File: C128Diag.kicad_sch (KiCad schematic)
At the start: 29 parts, among them U1 4066, U10 74LS04, U11 74LS04, U12 74LS10, U13 27128, U14 C64-Exp-Port, U2 4066, U3 4066, U4 NE555P, U5 74LS245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

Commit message: Tracing traces and reconstructing schematics.
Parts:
- added J1: CP1, Connector_PinHeader_2.54mm:PinHeader_1x05_P2.54mm_Vertical, symbol Connector_Generic:Conn_01x05
- added J2: CP2, Connector_PinHeader_2.54mm:PinHeader_1x05_P2.54mm_Vertical, symbol Connector_Generic:Conn_01x05
- added J3: KB, Connector_PinHeader_2.54mm:PinHeader_1x13_P2.54mm_Vertical, symbol Connector_Generic:Conn_01x13
- added JU1, JU2, JU3, JU4, JU5: Jumper_2_Open, C128Diag:Jumper, symbol Jumper:Jumper_2_Open
- added P1: 1k, Potentiometer_THT:Potentiometer_Bourns_3339P_Vertical, symbol Device:R_Potentiometer
- added R1: 150, Resistor_THT:R_Axial_DIN0309_L9.0mm_D3.2mm_P12.70mm_Horizontal, symbol Device:R_Small
- added R2: 330, Resistor_THT:R_Axial_DIN0309_L9.0mm_D3.2mm_P12.70mm_Horizontal, symbol Device:R_Small
- added R3, R4: 5k6, Resistor_THT:R_Axial_DIN0309_L9.0mm_D3.2mm_P12.70mm_Horizontal, symbol Device:R_Small
- C1: value C_Small -> 100n; footprint Capacitor_THT:C_Disc_D4.7mm_W2.5mm_P5.00mm -> C128Diag:Jumper
- C10, C11, C12, C13, C14, C15, C2, C4, C5, C6, C7, C8, C9: value C_Small -> 100n
- C3: value C_Small -> 10n
- U10, U11, U12, U9: footprint (none) -> Package_DIP:DIP-14_W7.62mm
- U14: footprint hackup:C64-Cart-NoSilkS -> C128Diag:C64-Cart-C128Diag
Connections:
- net +5V: now also U12.13, U13.1 (VPP), U13.27 (~{PGM}), U4.4 (R), R3.1
- net GND: now also C2.2, U13.20 (~{CE}), U14.1 (GND), U14.22 (GND), U6.1 (OE), JU3.1 (A), JU4.1 (A), P1.3
- net at C2.1: now also U4.2 (TR), U4.6 (THR), R4.2
- net at U4.3 (Q): now also P1.1
- net at U4.5 (CV): now also C3.1
- net at U4.7 (DIS): now also R3.2, R4.1
- net at U12.3: now also U11.12
- net at U12.4: now also U11.5
- net at U12.5: now also U12.9, U14.E (PHI2)
- net at U12.6: now also U6.11 (Cp)
- net at U5.19 (CE): now also U12.8
- net D0: now reaches U5.2 (A0)
- net D0: now also U13.11 (D0), U14.21 (D0), U6.3 (D0)
- net D1: now reaches U5.3 (A1)
- net D1: now also U13.12 (D1), U14.20 (D1), U6.4 (D1)
- net D2: now reaches U5.4 (A2)
- net D2: now also U13.13 (D2), U14.19 (D2), U6.7 (D2)
- net D3: now reaches U5.5 (A3)
- net D3: now also U13.15 (D3), U14.18 (D3), U6.8 (D3)
- net D4: now reaches U5.6 (A4)
- net D4: now also U13.16 (D4), U14.17 (D4), U6.13 (D4)
- net D5: now reaches U5.7 (A5)
- net D5: now also U13.17 (D5), U14.16 (D5), U6.14 (D5)
- net D6: now reaches U5.8 (A6)
- net D6: now also U13.18 (D6), U14.15 (D6), U6.17 (D6)
- net D7: now reaches U5.9 (A7)
- net D7: now also U13.19 (D7), U14.14 (D7), U6.18 (D7)
- net at U14.10 (/I/O2): now also U11.13, JU5.1 (A)
- net at U14.11 (/ROML): now also JU2.2 (B)
- net at U14.7 (/I/O1): now also U12.1
- net at U14.8 (/GAME): now also JU4.2 (B)
- net at U14.9 (/EXROM): now also JU3.2 (B), JU5.2 (B)
- net at U14.B (/ROMH): now also U12.2, JU1.2 (B)
- net A13: now reaches U14.J (A13)
- net A12: now reaches U14.K (A12)
- net A12: now also U13.2 (A12)
- net A11: now reaches U14.L (A11)
- net A11: now also U13.23 (A11)
- net A10: now reaches U14.M (A10)
- net A10: now also U13.21 (A10)
- net A9: now reaches U14.N (A9)
- net A9: now also U13.24 (A9)
- net A8: now reaches U14.P (A8)
- net A8: now also U13.25 (A8)
- net A7: now reaches U14.R (A7)
- net A7: now also U13.3 (A7)
- net A6: now reaches U14.S (A6)
- net A6: now also U13.4 (A6)
- net A5: now reaches U14.T (A5)
- net A5: now also U13.5 (A5)
- net A4: now reaches U14.U (A4)
- net A4: now also U13.6 (A4)
- net A3: now reaches U14.V (A3)
- net A3: now also U13.7 (A3)
- net A2: now reaches U14.W (A2)
- net A2: now also U13.8 (A2)
- net A1: now reaches U14.X (A1)
- net A1: now also U13.9 (A1)
- net A0: now reaches U14.Y (A0)
- net A0: now also U13.10 (A0)
- net /OE: now reaches U13.22 (~{OE})
- net /OE: now also JU1.1 (A), JU2.1 (A)
- net at U11.6: now also U12.10
- net at U12.12: now also U12.11
- net P1: now reaches U2.2 (Y1)
- net P1: now also P1.2
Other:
- moved on the sheet: C2, C3, U11C, U11F, U12A, U12B, U12C, U14, U5, U6

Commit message: Tracing traces and reconstructing schematics.
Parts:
- added J4: Cas, C128Diag:Cassete-C128Diag, symbol Connector_Generic:Conn_01x06
- C1: footprint C128Diag:Jumper -> Capacitor_THT:C_Disc_D4.7mm_W2.5mm_P5.00mm
- U9: value 74LS08 -> 74HC08
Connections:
- net D4: now also U6.18 (D7); no longer U6.13 (D4)
- net D5: now also U6.17 (D6); no longer U6.14 (D5)
- net D6: now also U6.14 (D5); no longer U6.17 (D6)
- net D7: now also U6.13 (D4); no longer U6.18 (D7)
- net GND: now also U5.1 (A->B)
- net at U11.1: now also U10.1, U10.5, U7.1, U7.13
- net at U11.2: now also U8.2
- net at U9.1: now also U10.8, U9.12
- net at U9.2: now also U10.11, U5.11 (B7), U6.12 (O4), U9.5
- net at U9.3: now also U7.9
- net at U9.11: now also U7.3, U8.12
- net at U9.13: now also U10.10, U9.10
- net at U10.9: now also U5.12 (B6), U6.15 (O5), U9.4, U9.9
- net at U7.2: now also U10.12
- net at U11.8: now also U8.9
- net at U11.9: now also U10.3, U7.10, U8.13
- net at U9.6: now also U7.12
- net at U7.4: now also U10.13
- net at U7.5: now also U8.8, U9.8
- net at U7.6: now also U10.6
- net at U5.15 (B3): now also U6.9 (O3)
- net at U10.2: now also U7.8
- net at U7.11: now also U10.4
- net at U11.10: now also U8.11
- net at U11.11: now also U8.10
- net at U8.1: now also J4.4 (Pin_4), J4.6 (Pin_6)
- no-connect marks 0 -> 3
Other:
- moved on the sheet: U10A, U10B, U10C, U10D, U10E, U10F, U11A, U11D, U11E, U7A, U7B, U7C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

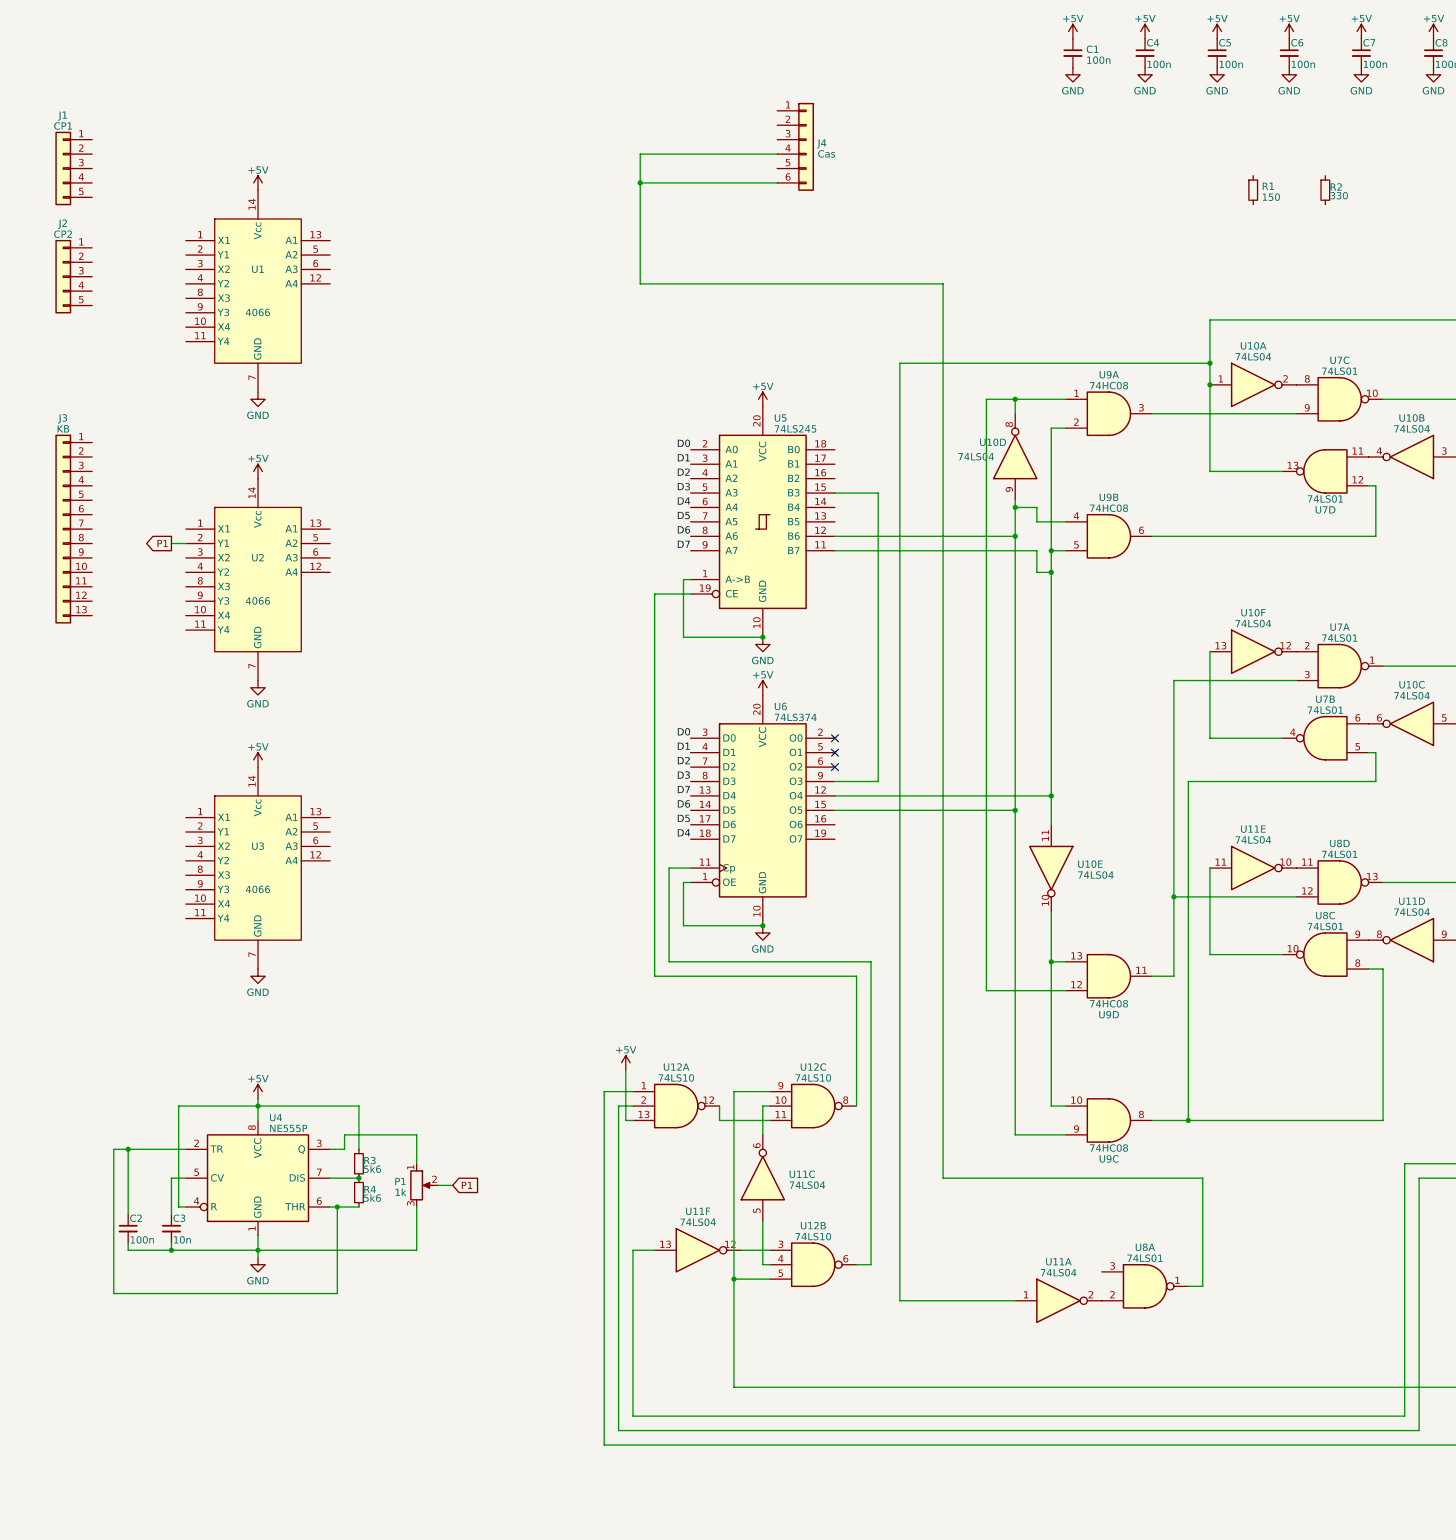
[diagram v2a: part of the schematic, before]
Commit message: Tracing traces and reconstructing schematics.
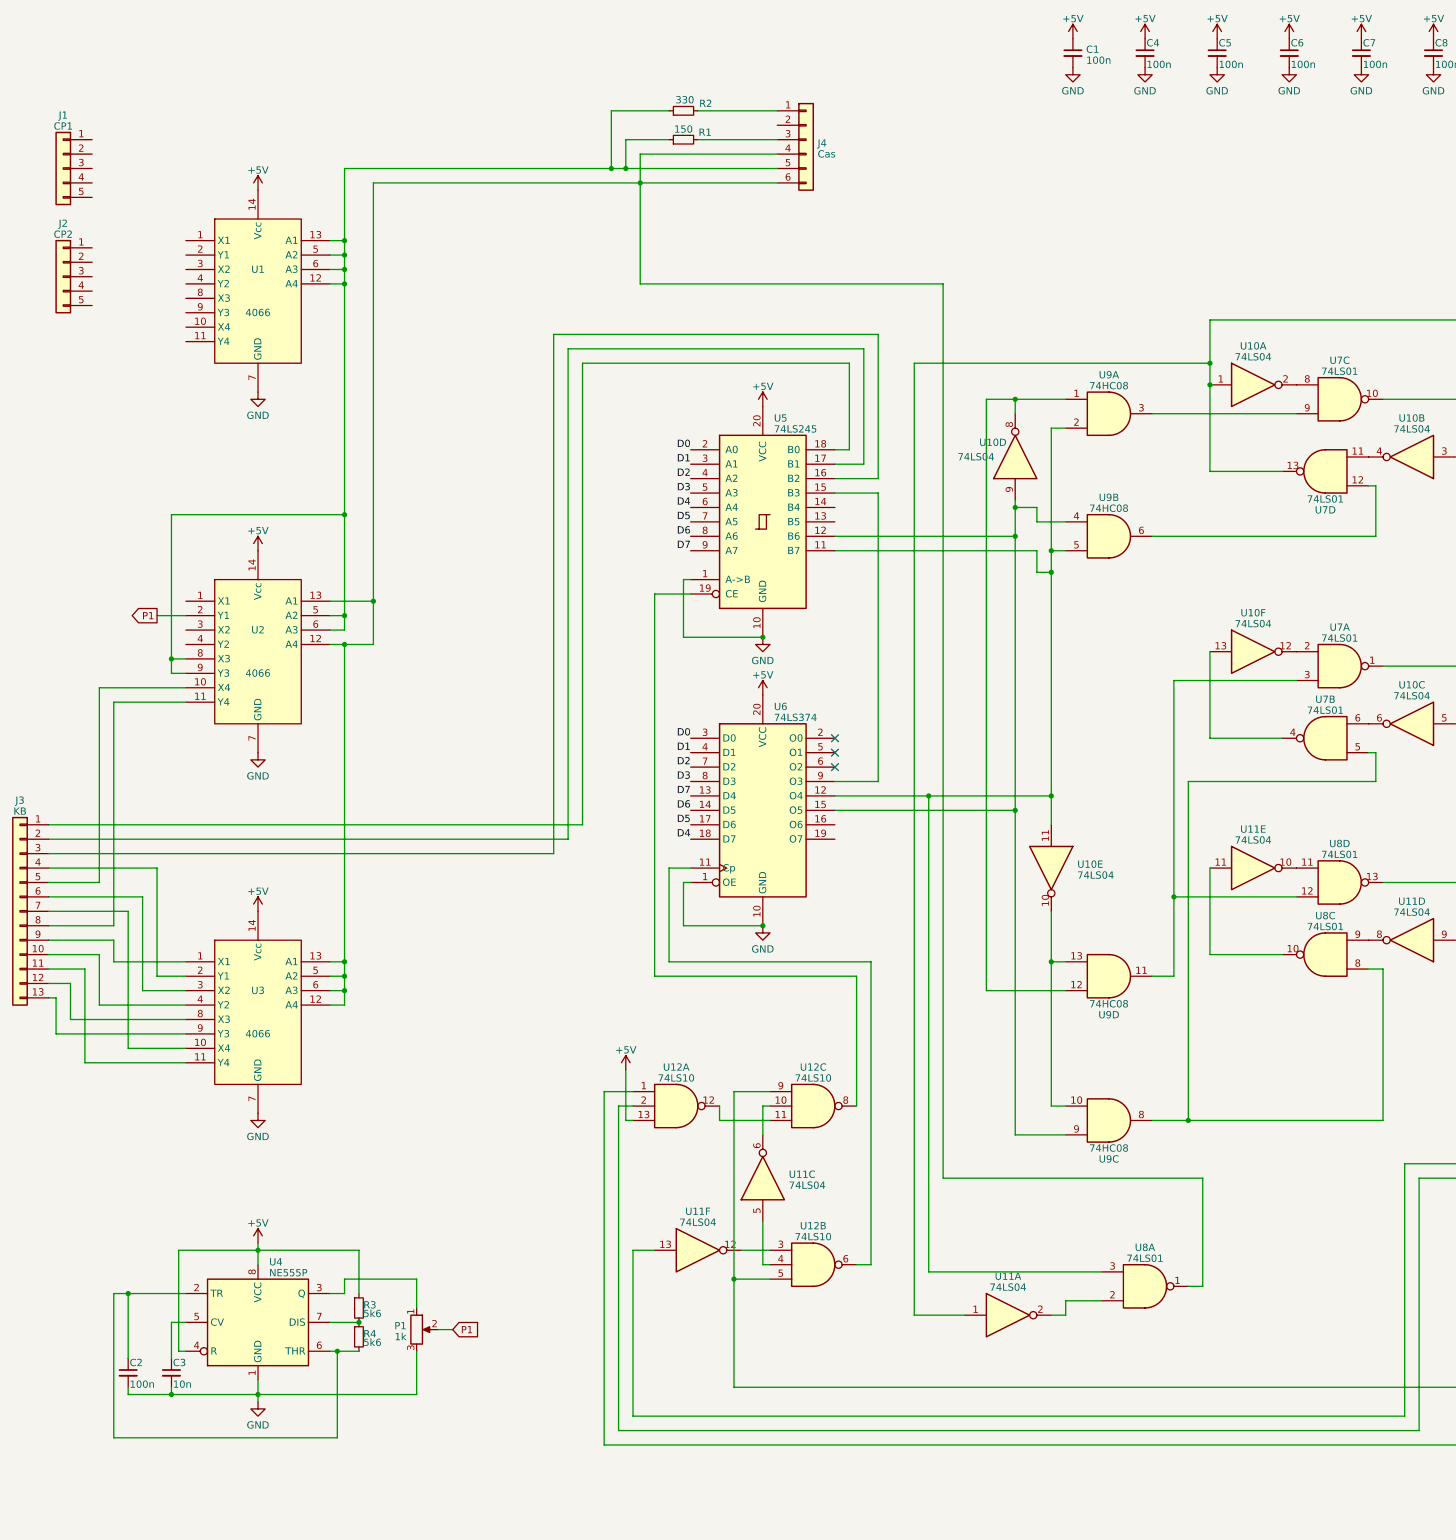
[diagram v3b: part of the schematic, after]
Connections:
- net at U10.11, U5.11 (B7), U6.12 (O4)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: now also U8.3
- net at J4.1 (Pin_1): now also R2.2
- net at J4.3 (Pin_3): now also R1.2
- net at J4.4 (Pin_4), J4.6 (Pin_6), U8.1: now also U2.12 (A4), U2.13 (A1), U3.12 (A4), U3.13 (A1), U3.5 (A2), U3.6 (A3)
- net at J4.5 (Pin_5): now also R1.1, R2.1, U1.12 (A4), U1.13 (A1), U1.5 (A2), U1.6 (A3), U2.5 (A2), U2.6 (A3), U2.8 (X3), U2.9 (Y3)
- net at U3.1 (X1): now also J3.9 (Pin_9)
- net at U3.10 (X4): now also J3.7 (Pin_7)
- net at U3.11 (Y4): now also J3.11 (Pin_11)
- net at U3.2 (Y1): now also J3.4 (Pin_4)
- net at U3.3 (X2): now also J3.6 (Pin_6)
- net at U3.4 (Y2): now also J3.10 (Pin_10)
- net at U3.8 (X3): now also J3.12 (Pin_12)
- net at U3.9 (Y3): now also J3.13 (Pin_13)
- net at U5.16 (B2): now also J3.3 (Pin_3)
- net at U5.17 (B1): now also J3.2 (Pin_2)
- net at U5.18 (B0): now also J3.1 (Pin_1)
- net at J3.5 (Pin_5): now also U2.10 (X4)
- net at J3.8 (Pin_8): now also U2.11 (Y4)
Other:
- moved on the sheet: C2, C3, J3, P1, R1, R2, R3, R4, U11A, U2, U3, U4

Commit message: Tracing traces and reconstructing schematics.
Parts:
- added H1, H10, H11, H12, H13, H14, H2, H3, H4, H5, H6, H7, H8, H9: MountingHole, C128Diag:Hole_3.2mm, symbol Mechanical:MountingHole
- added J5: Vid, Connector_PinHeader_2.54mm:PinHeader_1x01_P2.54mm_Vertical, symbol Connector_Generic:Conn_01x01
- added J6: Serial, C128Diag:PinHeader_1x02_P5.08mm_Vertical, symbol Connector_Generic:Conn_01x02
- added J7: UP, C128Diag:PinHeader_1x02_P5.08mm_Vertical, symbol Connector_Generic:Conn_01x02
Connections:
- net A13: now also U13.26 (A13)
- net at U10.1, U10.5, U11.1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: now also J6.1 (Pin_1)
- net at U11.5, U12.4: now also U11.4
- net at U10.3, U11.9, U7.10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: now also J6.2 (Pin_2)
- net at U10.13, U7.4: now also J7.1 (Pin_1)
- net at U1.1 (X1): now also J1.1 (Pin_1)
- net at U1.10 (X4): now also J2.3 (Pin_3)
- net at U1.11 (Y4): now also J1.3 (Pin_3)
- net at U1.2 (Y1): now also J2.1 (Pin_1)
- net at U1.3 (X2): now also J2.2 (Pin_2)
- net at U1.4 (Y2): now also J1.2 (Pin_2)
- net at U1.8 (X3): now also J1.4 (Pin_4)
- net at U1.9 (Y3): now also J2.4 (Pin_4)
- net at U5.13 (B5): now also U6.16 (O6)
- net at U5.14 (B4): now also U6.19 (O7)
- net at U14.5 (R-/W): now also U11.3
- net at J2.5 (Pin_5): now also U2.3 (X2)
- net at U11.11, U8.10: now also J7.2 (Pin_2)
- net at J1.5 (Pin_5): now also U2.4 (Y2)
- net at U2.1 (X1): now also J5.1 (Pin_1)
- net P1: no longer names the net of P1.2, U2.2 (Y1)
- no-connect marks 3 -> 12
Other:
- moved on the sheet: J1, J2, J4, JU1, JU2, JU3, JU4, JU5, R1, R2, U10G, U11B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
